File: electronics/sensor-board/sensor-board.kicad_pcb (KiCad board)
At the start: 4 copper layers, 270 x 30 mm, 155 parts, among them J1 Load Cell Input, J10 Load Cell Input, J11 FSR Input, J12 Digital Input, J13 Conn_02x04_Odd_Even, J14 Conn_02x04_Odd_Even, J15 Conn_01x06_Male, J16 USB_C_Receptacle_USB2.0, J17 Conn_02x04_Odd_Even, J18 Barrel_Jack_MountingPin, J2 FSR Input, J3 Digital Input, J4 Load Cell Input, J5 FSR Input, J6 Digital Input, J7 Load Cell Input, J8 FSR Input, J9 Digital Input, U1 LMV321, U10 TJA1042T-3, U11 74HCT245, U12 AMS1117-3.3, U13 TPS5430DDA, U2 INA826, U3 LMV321, U4 INA826, U5 LMV321, U6 INA826, U7 LMV321, U8 INA826, U9 STM32G431CBT6, Y1 8MHz

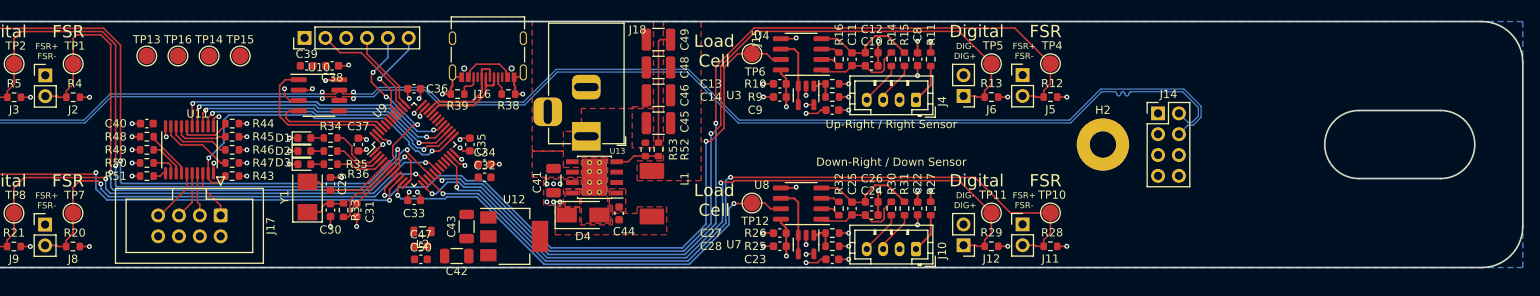
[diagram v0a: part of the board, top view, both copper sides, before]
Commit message: Finish routing for v3.01
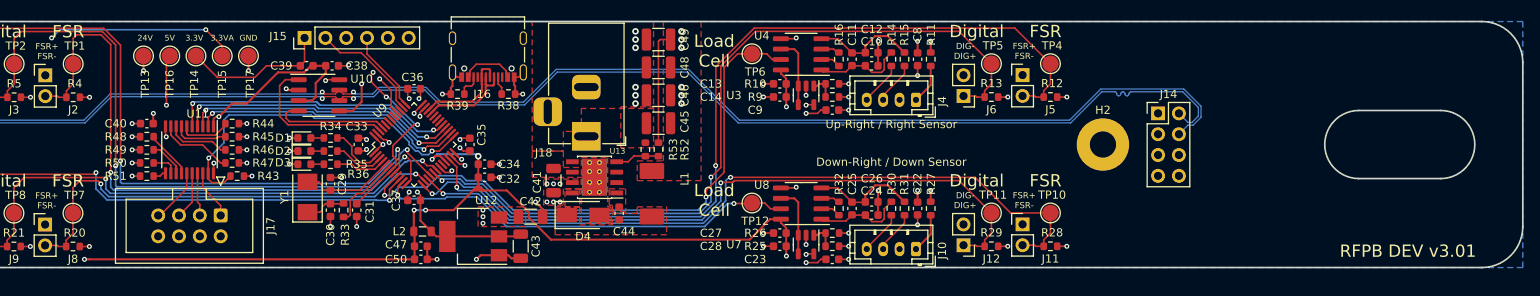
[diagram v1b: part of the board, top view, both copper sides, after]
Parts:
- added TP17: TestPoint, TestPoint:TestPoint_Pad_D2.0mm, F.Cu at (192.2, 127.6)
- moved C42 10.2 mm to (226.6, 147.2), turned to 0 degrees
- moved C33 9.62 mm to (205.6, 138.4), turned to 90 degrees
- moved C37 9.62 mm to (212.4, 145.2), turned to 180 degrees
- moved C43 7.02 mm to (225.4, 150.8), turned to -90 degrees
- moved U12 5.00 mm to (219.6, 149.6), turned to 180 degrees
- moved TP15 2.20 mm to (189.0, 127.6)
- moved TP14 1.60 mm to (185.8, 127.6)
- moved TP16 1.00 mm to (182.6, 127.6)
- moved R43 0.61 mm to (190.8, 142.2)
- moved TP13 0.40 mm to (179.4, 127.6)
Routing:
- net +3.3VA: track 54.0 -> 188.6 mm, vias 28 -> 35
- net +3.3V: track 10.3 -> 49.4 mm, vias 7 -> 8
- net +5V: track 20.7 -> 47.3 mm, vias 4 -> 14
- net GND: track 96.0 -> 111.1 mm, vias 65 -> 77
- net /controller/LOADCELL_UR: track 76.3 -> 70.6 mm
- net /controller/DIGITALSENSOR_DR: track 88.4 -> 82.9 mm
- net /controller/DIGITALSENSOR_UR: track 102.5 -> 97.1 mm
- net /controller/FSR_DR: track 96.2 -> 90.7 mm
- net /controller/FSR_UR: track 112.8 -> 107.4 mm
- net /controller/LOADCELL_DR: track 56.8 -> 51.9 mm
- net +24V: track 0.00 -> 1.80 mm, vias 6 -> 7
- net /controller/LED_EN: track 42.1 -> 42.7 mm
- added copper zone on In2.Cu, net +3.3V
- added copper zone on In2.Cu, net +3.3VA
- added copper zone on In2.Cu, net +5V
- added copper zone on In1.Cu, net GND
- removed copper zone on In1.Cu, net +3.3V
- removed copper zone on In1.Cu, net +3.3VA
- removed copper zone on In1.Cu, net +5V
- removed copper zone on In2.Cu, net GND
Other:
- board text added: "24V"
- board text added: "3.3V"
- board text added: "3.3VA"
- board text added: "5V"
- board text added: "GND"
- board text added: "RFPB DEV v3.01"
